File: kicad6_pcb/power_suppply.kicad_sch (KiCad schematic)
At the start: 24 parts, among them J201 Barrel_Jack, J202 GND, J203 DC Power, J204 -8V, J205 +8V, U201 LM317L, U202 UA78M08, U203 UA79M08, U204 TLE2426xP

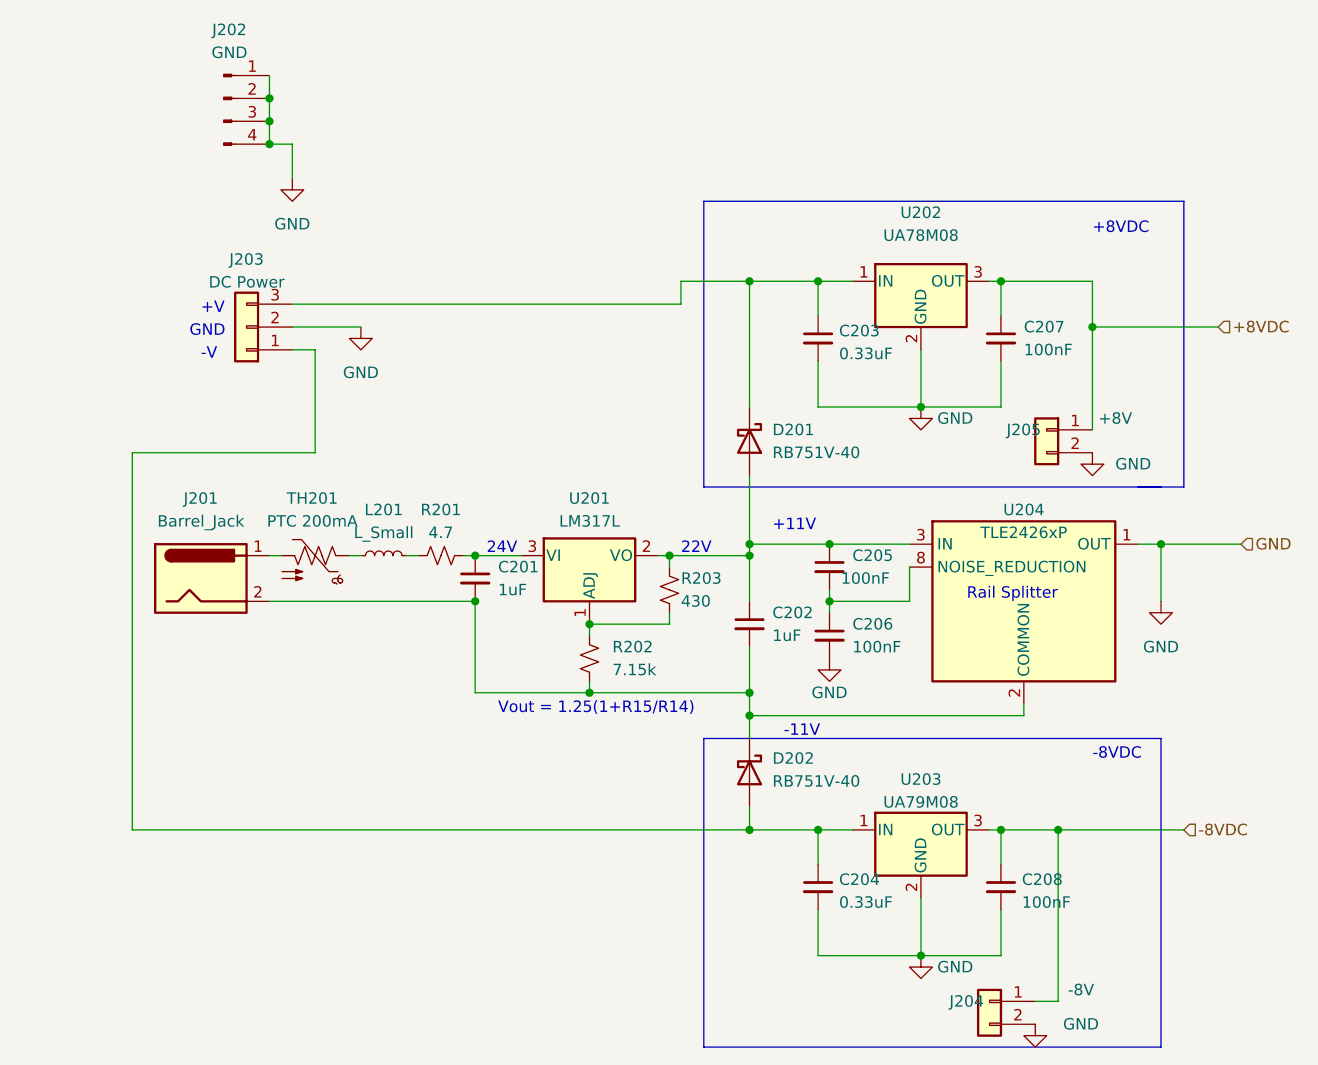
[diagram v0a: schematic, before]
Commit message: CSA carrier v2. Multiple fixes and improvements.
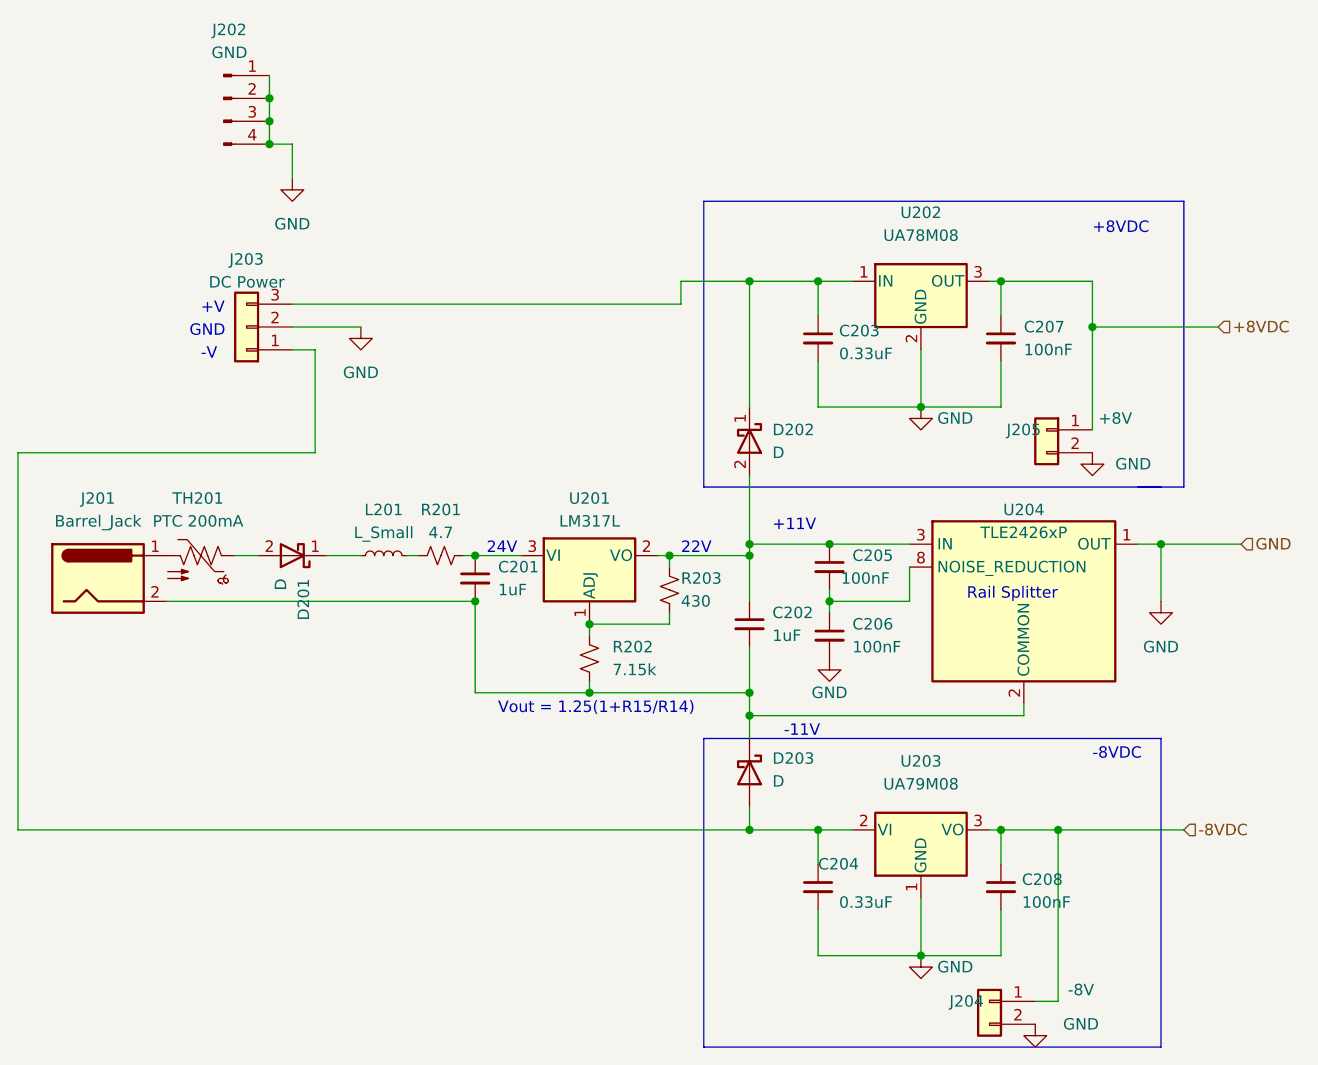
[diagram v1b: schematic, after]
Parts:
- added D201: D, Diode_SMD:D_SOD-123, symbol Device:D_Schottky
- D202: renamed from D201; value RB751V-40 -> D; footprint Diode_SMD:D_SOD-523 -> Diode_SMD:D_SOD-123; Digikey 3757-RB751V-40-AU_R1_000A1CT-ND -> (none); Mouser 241-RB751V-40R100001 -> 755-RBR2L40ADDTE25
- D203: renamed from D202; value RB751V-40 -> D; footprint Diode_SMD:D_SOD-523 -> Diode_SMD:D_SOD-123; Digikey 3757-RB751V-40-AU_R1_000A1CT-ND -> (none); Mouser 241-RB751V-40R100001 -> 755-RBR2L40ADDTE25
- J201: footprint Connector_PinHeader_2.54mm:PinHeader_1x02_P2.54mm_Vertical -> Connector_Wire:SolderWire-0.75sqmm_1x02_P4.8mm_D1.25mm_OD2.3mm
- U203: symbol Regulator_Linear:uA7808 -> Regulator_Linear:LM7908_TO220
- U204: Mouser 595-TLE2426MDREP -> 595-TLE2426MD
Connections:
- net GND: now also U203.1 (GND); no longer U203.2 (GND)
- net at C204.1, D203.2 (A), J203.1 (Pin_1): now also U203.2 (VI); no longer U203.1 (IN)
- net at TH201.1: now also D201.2 (A); no longer L201.1
- new net: D201.1 (K), L201.1
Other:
- moved on the sheet: J201, TH201
